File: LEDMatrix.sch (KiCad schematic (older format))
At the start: 69 parts, among them SW1 SW_Push_LED, SW10 SW_Push_LED, SW11 SW_Push_LED, SW12 SW_Push_LED, SW13 SW_Push_LED, SW14 SW_Push_LED, SW15 SW_Push_LED, SW16 SW_Push_LED, SW17 SW_Push_LED, SW18 SW_Push_LED, SW19 SW_Push_LED, SW2 SW_Push_LED, SW20 SW_Push_LED, SW21 SW_Push_LED, SW22 SW_Push_LED, SW23 SW_Push_LED, SW24 SW_Push_LED, SW25 SW_Push_LED, SW26 SW_Push_LED, SW27 SW_Push_LED, SW28 SW_Push_LED, SW29 SW_Push_LED, SW3 SW_Push_LED, SW30 SW_Push_LED, SW31 SW_Push_LED, SW32 SW_Push_LED, SW33 SW_Push_LED, SW34 SW_Push_LED, SW35 SW_Push_LED, SW36 SW_Push_LED, SW37 SW_Push_LED, SW38 SW_Push_LED, SW39 SW_Push_LED, SW4 SW_Push_LED, SW40 SW_Push_LED, SW41 SW_Push_LED, SW42 SW_Push_LED, SW43 SW_Push_LED, SW44 SW_Push_LED, SW45 SW_Push_LED, SW46 SW_Push_LED, SW47 SW_Push_LED, SW48 SW_Push_LED, SW49 SW_Push_LED, SW5 SW_Push_LED, SW50 SW_Push_LED, SW51 SW_Push_LED, SW52 SW_Push_LED, SW53 SW_Push_LED, SW54 SW_Push_LED, SW55 SW_Push_LED, SW56 SW_Push_LED, SW57 SW_Push_LED, SW58 SW_Push_LED, SW59 SW_Push_LED, SW6 SW_Push_LED, SW60 SW_Push_LED, SW61 SW_Push_LED, SW62 SW_Push_LED, SW63 SW_Push_LED, SW64 SW_Push_LED, SW65 SW_Push_LED, SW66 SW_Push_LED, SW67 SW_Push_LED, SW68 SW_Push_LED, SW69 SW_Push_LED, SW7 SW_Push_LED, SW8 SW_Push_LED, SW9 SW_Push_LED

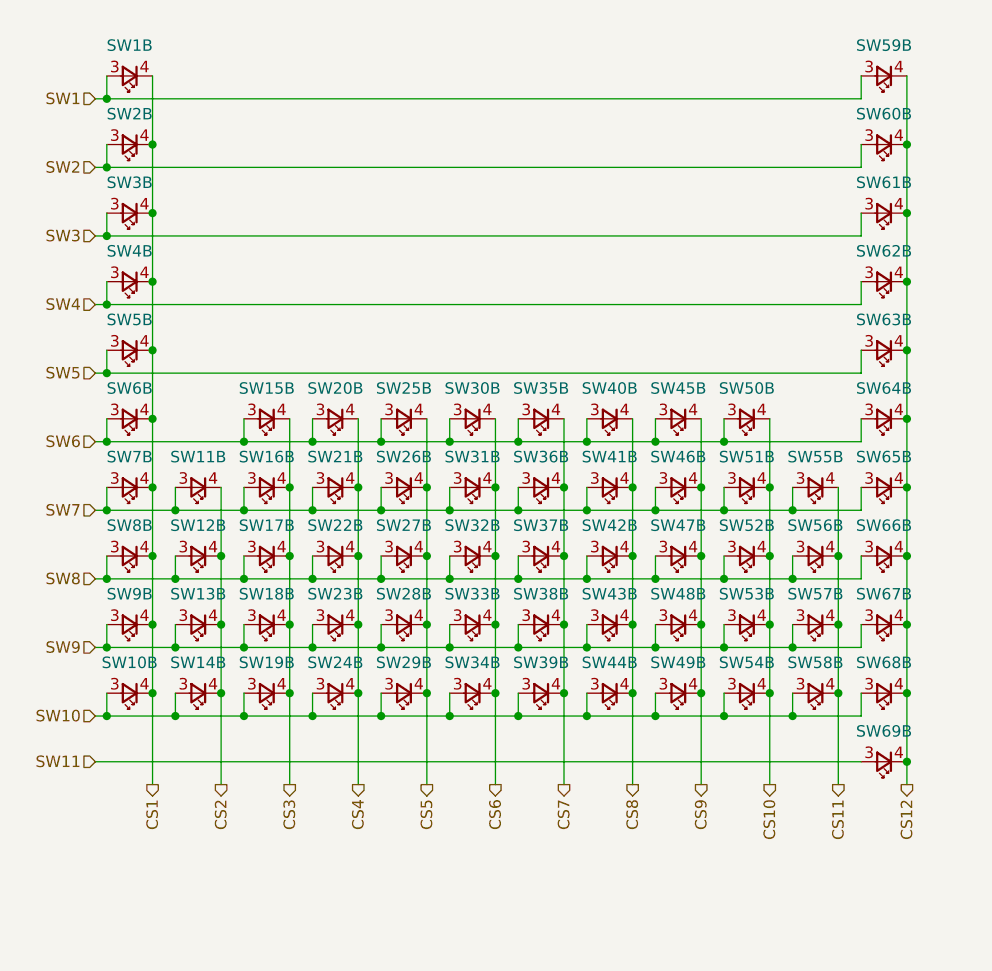
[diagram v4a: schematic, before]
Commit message: Fix the button layout. Still needs trace work.
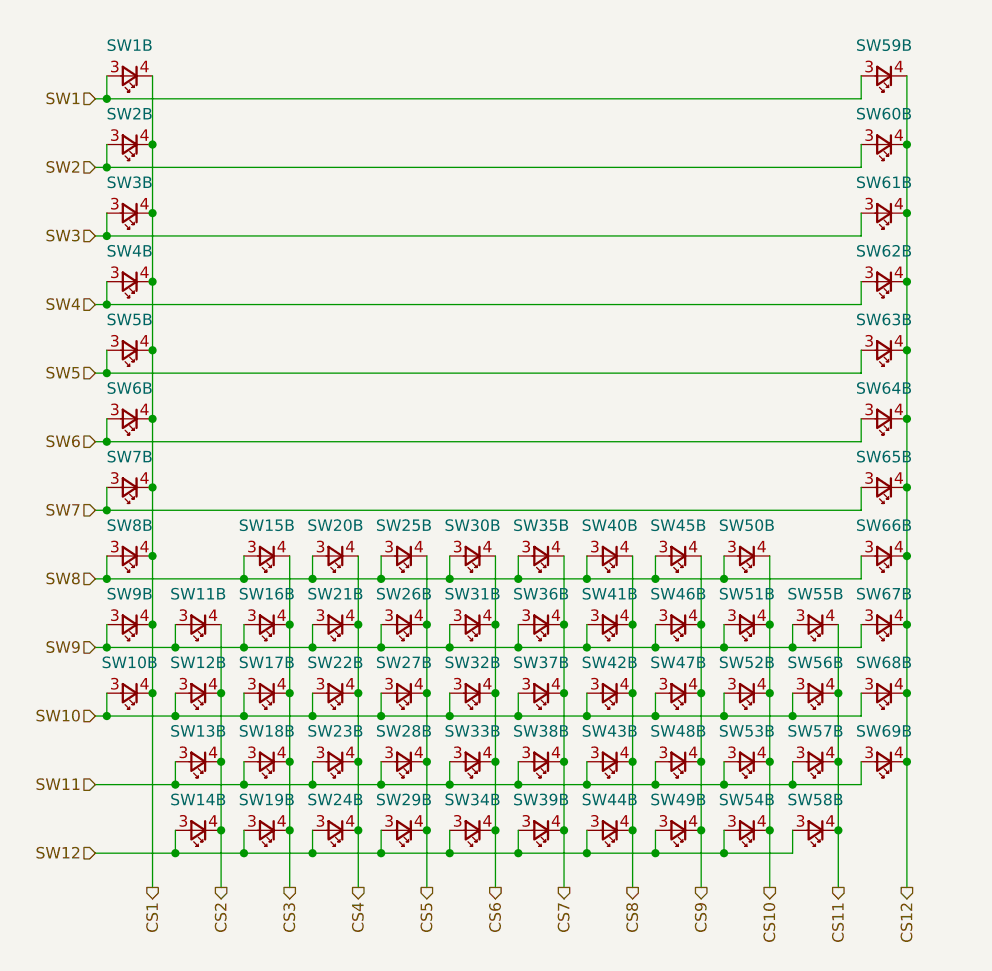
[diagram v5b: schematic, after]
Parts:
- removed SW10, SW68, SW69, SW9: SW_Push_LED, Collins-FMS-3000:SW_PUSH_6mm, symbol Collins-FMS-3000:SW_Push_LED
- added SW6, SW64, SW65, SW7: SW_Push_LED, Collins-FMS-3000:SW_PUSH_6mm, symbol Collins-FMS-3000:SW_Push_LED
- renumbered SW8 to SW10, SW64 to SW66, SW65 to SW67, SW66 to SW68, SW67 to SW69, SW6 to SW8, SW7 to SW9
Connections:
- net CS1: now also SW6.4, SW7.4
- net CS12: now also SW64.4, SW65.4
- net SW10: now also SW10.3, SW12.3, SW17.3, SW22.3, SW27.3, SW32.3, SW37.3, SW42.3, SW47.3, SW52.3, SW56.3, SW68.3; no longer SW14.3, SW19.3, SW24.3, SW29.3, SW34.3, SW39.3, SW44.3, SW49.3, SW54.3, SW58.3
- net SW11: now also SW13.3, SW18.3, SW23.3, SW28.3, SW33.3, SW38.3, SW43.3, SW48.3, SW53.3, SW57.3, SW69.3
- net SW6: now also SW6.3, SW64.3; no longer SW15.3, SW20.3, SW25.3, SW30.3, SW35.3, SW40.3, SW45.3, SW50.3, SW66.3, SW8.3
- net SW7: now also SW65.3, SW7.3; no longer SW11.3, SW16.3, SW21.3, SW26.3, SW31.3, SW36.3, SW41.3, SW46.3, SW51.3, SW55.3, SW67.3, SW9.3
- net SW8: now also SW15.3, SW20.3, SW25.3, SW30.3, SW35.3, SW40.3, SW45.3, SW50.3, SW66.3, SW8.3; no longer SW10.3, SW12.3, SW17.3, SW22.3, SW27.3, SW32.3, SW37.3, SW42.3, SW47.3, SW52.3, SW56.3, SW68.3
- net SW9: now also SW11.3, SW16.3, SW21.3, SW26.3, SW31.3, SW36.3, SW41.3, SW46.3, SW51.3, SW55.3, SW67.3, SW9.3; no longer SW13.3, SW18.3, SW23.3, SW28.3, SW33.3, SW38.3, SW43.3, SW48.3, SW53.3, SW57.3, SW69.3
- new net SW12: SW14.3, SW19.3, SW24.3, SW29.3, SW34.3, SW39.3, SW44.3, SW49.3, SW54.3, SW58.3
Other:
- moved on the sheet: SW10B, SW11B, SW12B, SW13B, SW14B, SW15B, SW16B, SW17B, SW18B, SW19B, SW20B, SW21B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
